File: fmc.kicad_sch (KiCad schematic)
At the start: 3 parts, among them J1 SAMTEC_ASP-134604-01, U1 M24C02-FMN

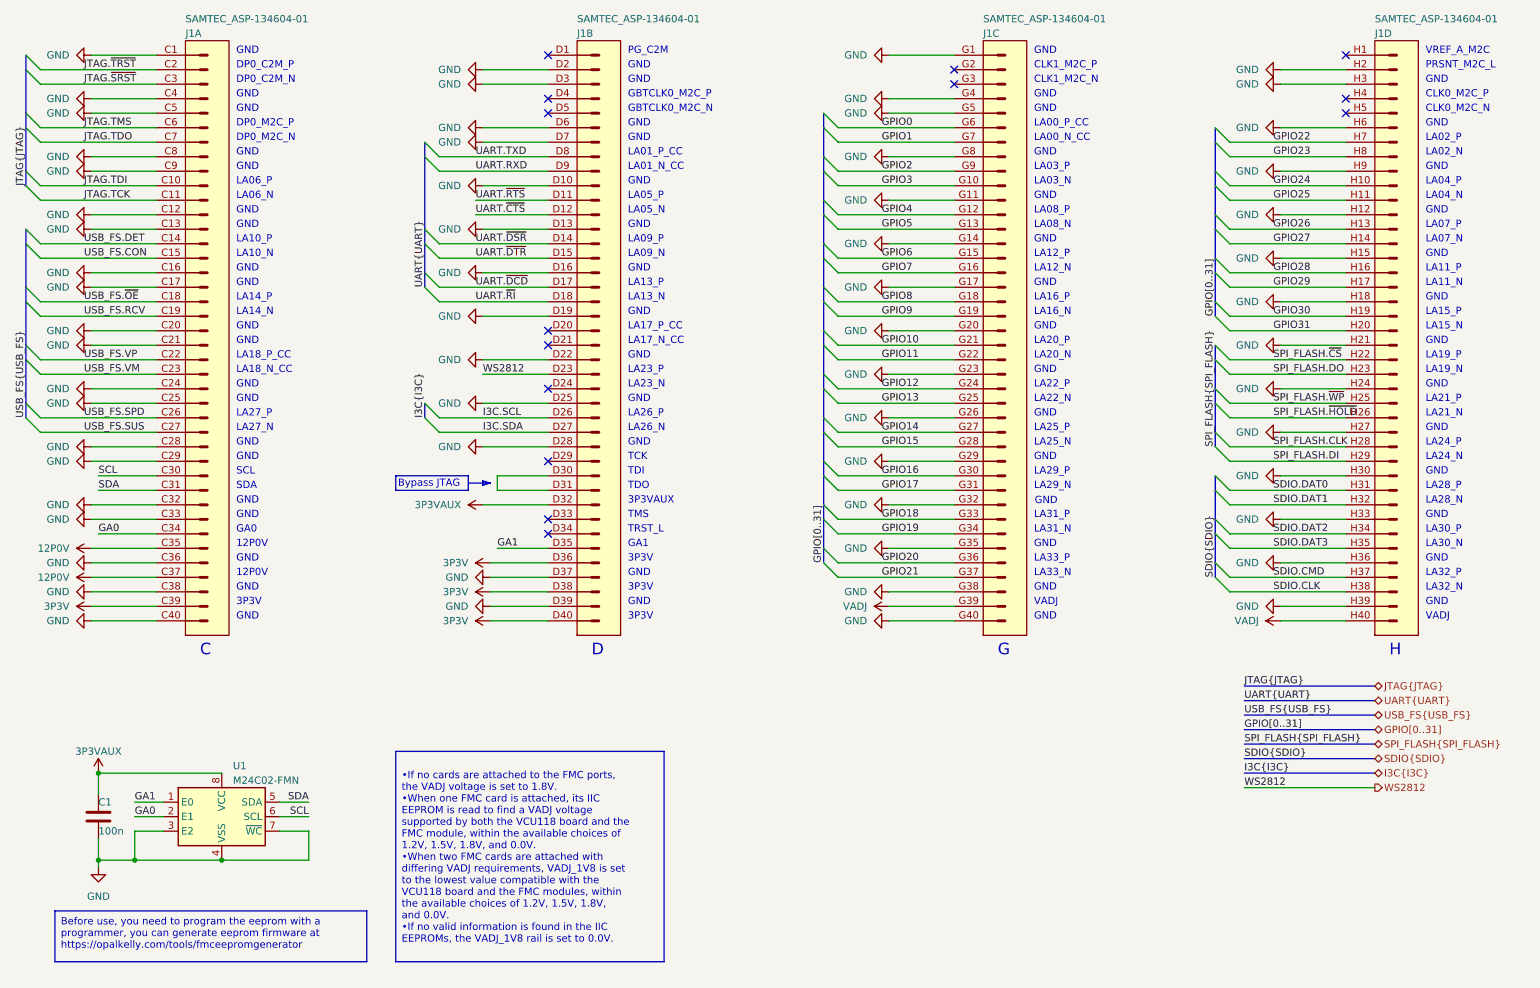
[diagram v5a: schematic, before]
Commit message: *.kicad_sch: connect GX0011 thermometer sensor
Signed-off-by: Huang Rui <vowstar@gmail.com>
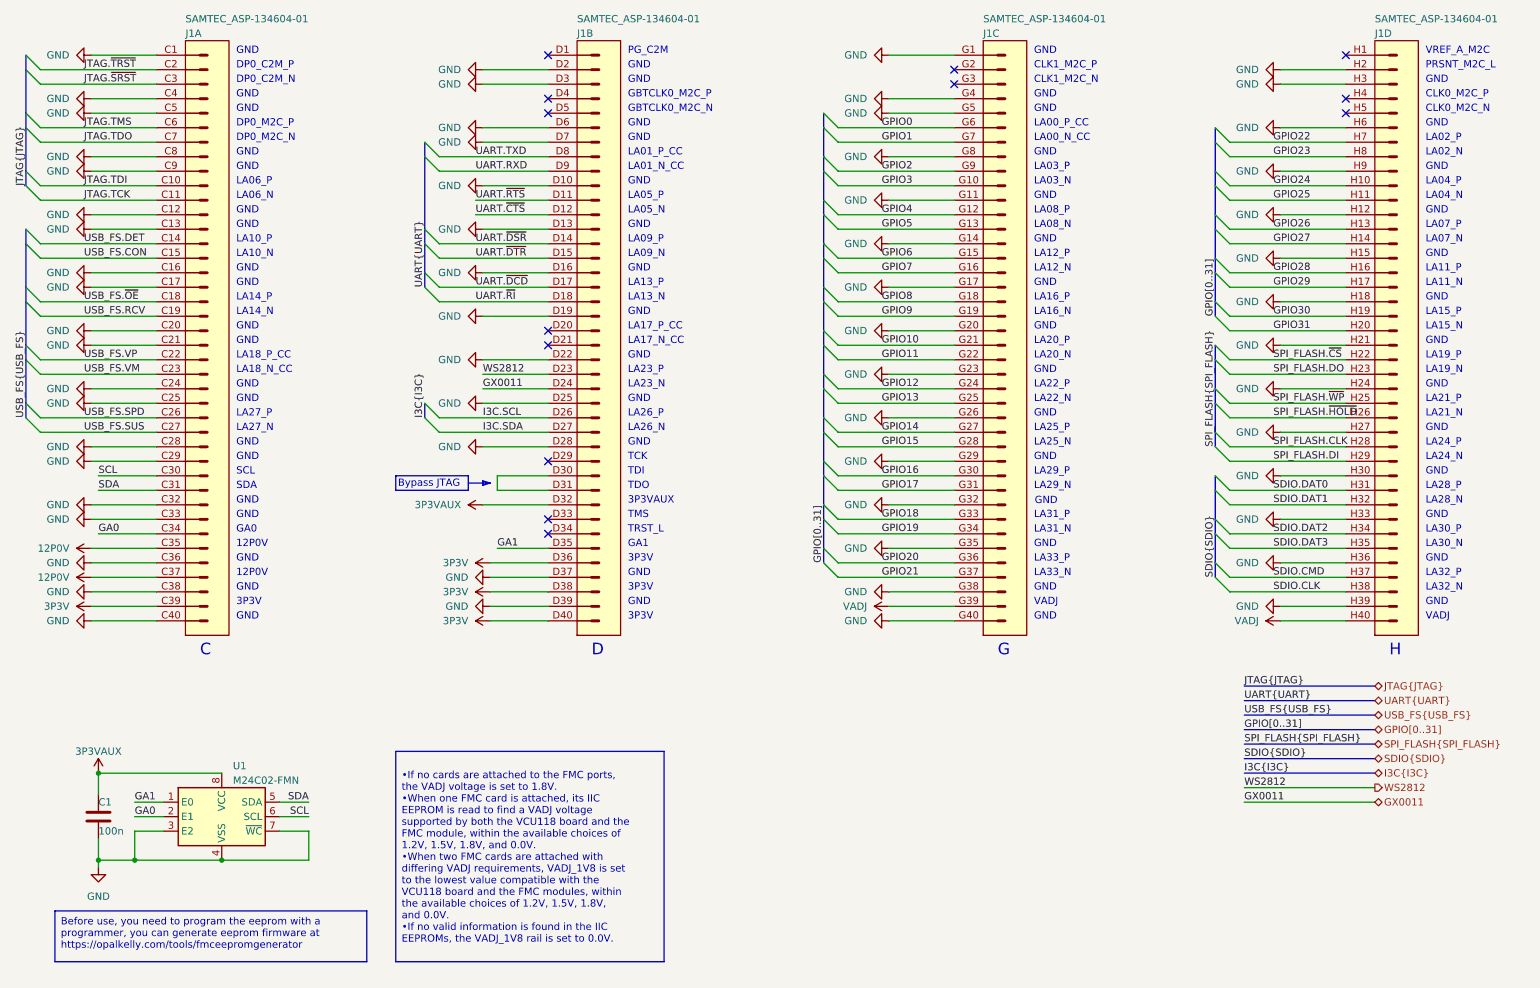
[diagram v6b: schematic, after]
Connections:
- net GX0011: now reaches J1.D24 (d24)
- no-connect marks 14 -> 13
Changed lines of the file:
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@@
   (no_connect (at 114.3 76.2))
   (no_connect (at 254 27.94))
-  (no_connect (at 114.3 86.36))
   (no_connect (at 114.3 35.56))
   (no_connect (at 114.3 27.94))
@@
     (stroke (width 0) (type default))
   )
+  (wire (pts (xy 102.87 86.36) (xy 114.3 86.36))
+    (stroke (width 0) (type default))
+  )
   (wire (pts (xy 242.57 48.26) (xy 254 48.26))
     (stroke (width 0) (type default))
@@
   )
   (wire (pts (xy 104.14 127) (xy 114.3 127))
+    (stroke (width 0) (type default))
+  )
+  (wire (pts (xy 236.22 158.75) (xy 259.08 158.75))
     (stroke (width 0) (type default))
   )
@@
     (effects (font (size 1.27 1.27)) (justify left bottom))
   )
+  (label "GX0011" (at 236.22 158.75 0) (fields_autoplaced)
+    (effects (font (size 1.27 1.27)) (justify left bottom))
+  )
   (label "GPIO[0..31]" (at 162.56 116.84 90) (fields_autoplaced)
     (effects (font (size 1.27 1.27)) (justify left bottom))
@@
     (effects (font (size 1.27 1.27)) (justify left bottom))
   )
+  (label "GX0011" (at 102.87 86.36 0) (fields_autoplaced)
+    (effects (font (size 1.27 1.27)) (justify left bottom))
+  )
   (label "GA1" (at 41.91 158.75 0) (fields_autoplaced)
     (effects (font (size 1.27 1.27)) (justify left bottom))
@@
     (effects (font (size 1.27 1.27)) (justify left))
   )
+  (hierarchical_label "GX0011" (shape bidirectional) (at 259.08 158.75 0) (fields_autoplaced)
+    (effects (font (size 1.27 1.27)) (justify left))
+  )
